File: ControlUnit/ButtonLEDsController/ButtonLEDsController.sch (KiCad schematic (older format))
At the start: 37 parts, among them J1 Conn_01x02_Female, Q1 IRLZ34N, T1 -PNP-2C-BCE, T10 MPSA42-NPN-TO92-CBE, T2 MPSA42-NPN-TO92-CBE, T3 MPSA42-NPN-TO92-CBE, T4 MPSA42-NPN-TO92-CBE, T5 MPSA42-NPN-TO92-CBE, T6 MPSA42-NPN-TO92-CBE, T7 MPSA42-NPN-TO92-CBE, T8 MPSA42-NPN-TO92-CBE, T9 MPSA42-NPN-TO92-CBE, U1 NodeMCU1.0(ESP-12E)

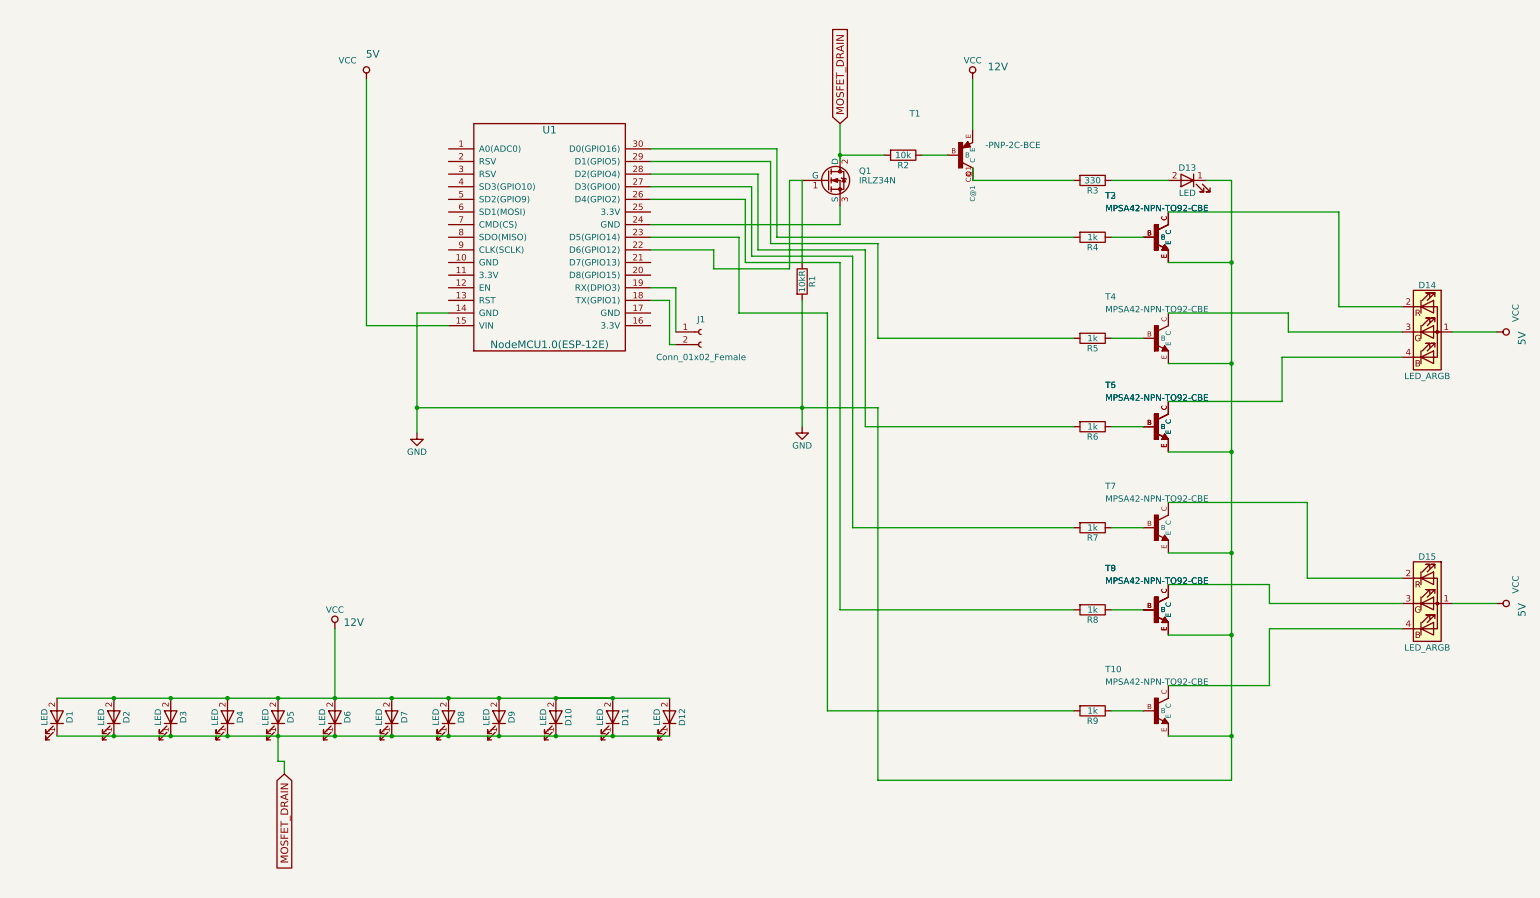
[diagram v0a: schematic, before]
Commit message: transistors in schematic taken from 3rd party lib were bad idea because default kicad footprints wouldn't match the pin references in the schematic (were E,B,C - needed to be 1,2,3 instead)
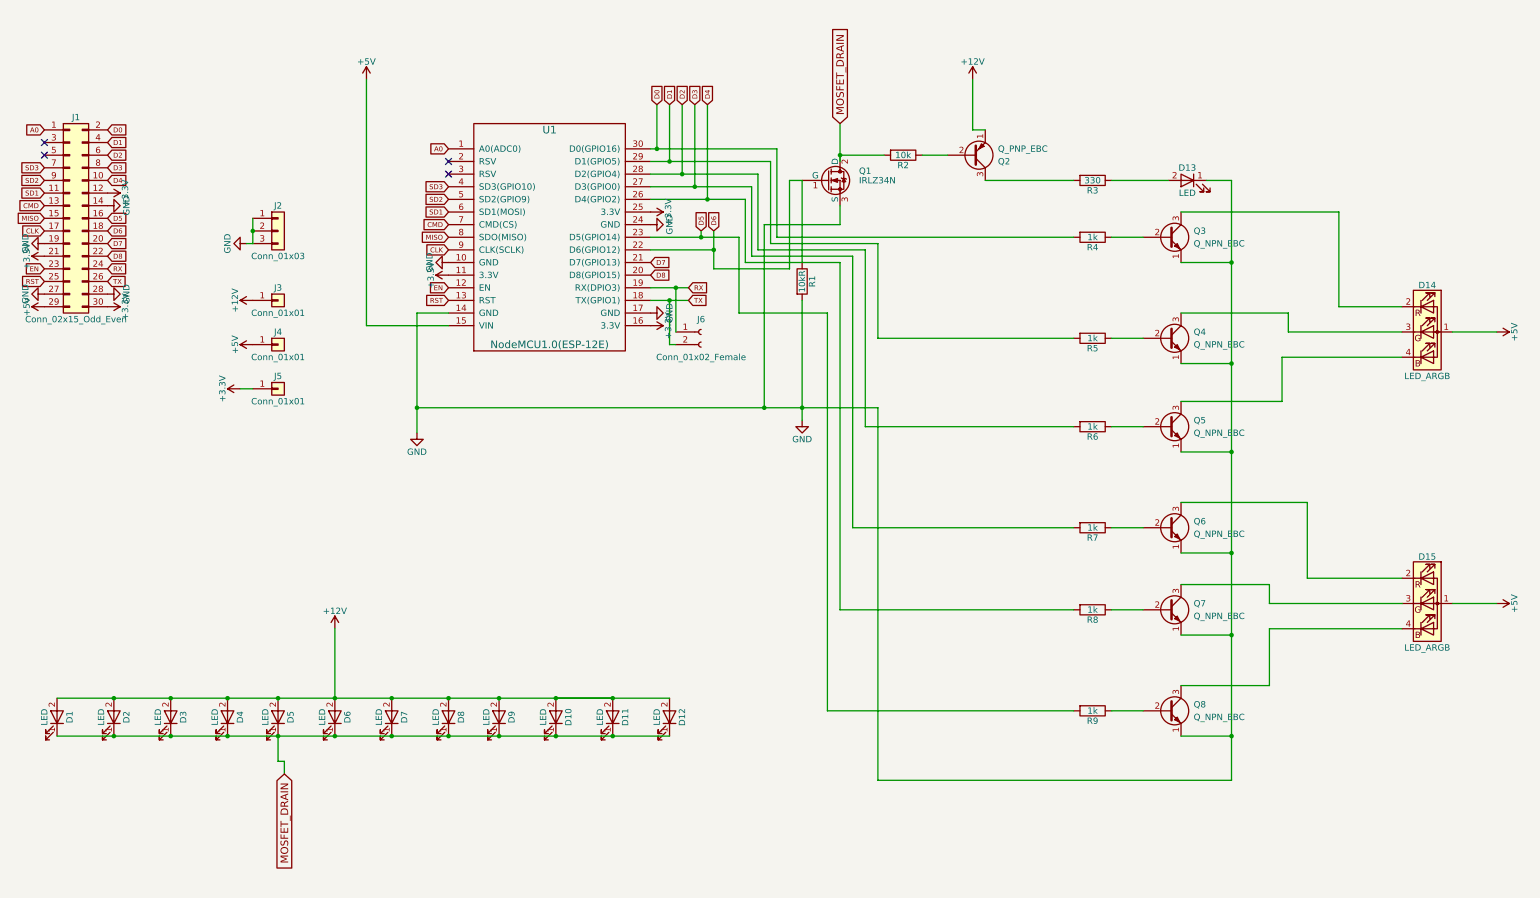
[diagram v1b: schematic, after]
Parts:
- removed T1: -PNP-2C-BCE, transistor-SOT89-BCE, symbol -PNP-2C-BCE
- removed T10, T2, T3, T4, T5, T6, T7, T8, T9: MPSA42-NPN-TO92-CBE, transistor-TO92-CBE, symbol MPSA42-NPN-TO92-CBE
- added J1: Conn_02x15_Odd_Even, Pin_Headers:Pin_Header_Straight_2x15_Pitch2.54mm, symbol Conn_02x15_Odd_Even
- added J2: Conn_01x03, Pin_Headers:Pin_Header_Straight_1x03_Pitch2.54mm, symbol Conn_01x03
- added J3, J4, J5: Conn_01x01, Pin_Headers:Pin_Header_Straight_1x01_Pitch2.54mm, symbol Conn_01x01
- added Q2: Q_PNP_EBC, TO_SOT_Packages_THT:TO-92_Molded_Narrow, symbol Q_PNP_EBC
- added Q3, Q4, Q5, Q6, Q7, Q8: Q_NPN_EBC, TO_SOT_Packages_THT:TO-92_Molded_Narrow, symbol Q_NPN_EBC
- J6: renamed from J1; footprint Socket_Strips:Socket_Strip_Straight_1x02_Pitch2.00mm -> Socket_Strips:Socket_Strip_Straight_1x02_Pitch2.54mm
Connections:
- net GND: now also Q1.3 (S), U1.10 (GND), U1.17 (GND), U1.24 (GND), J1.14 (Pin_14), J1.19 (Pin_19), J1.27 (Pin_27), J1.28 (Pin_28), J2.1 (Pin_1), J2.2 (Pin_2), J2.3 (Pin_3), Q3.1 (E), Q4.1 (E), Q5.1 (E), Q6.1 (E), Q7.1 (E), Q8.1 (E)
- net A0: now reaches U1.1 (A0(ADC0))
- net A0: now also J1.1 (Pin_1)
- net +3V3: now reaches U1.11 (3.3V)
- net +3V3: now also U1.16 (3.3V), U1.25 (3.3V), J1.12 (Pin_12), J1.21 (Pin_21), J1.30 (Pin_30), J5.1 (Pin_1)
- net EN: now reaches U1.12 (EN)
- net EN: now also J1.23 (Pin_23)
- net RST: now reaches U1.13 (RST)
- net RST: now also J1.25 (Pin_25)
- net TX: now reaches J6.2 (Pin_2), U1.18 (TX(GPIO1))
- net TX: now also J1.26 (Pin_26)
- net RX: now reaches J6.1 (Pin_1), U1.19 (RX(DPIO3))
- net RX: now also J1.24 (Pin_24)
- net D8: now reaches U1.20 (D8(GPIO15))
- net D8: now also J1.22 (Pin_22)
- net D7: now reaches U1.21 (D7(GPIO13))
- net D7: now also J1.20 (Pin_20)
- net D6: now reaches Q1.1 (G), R1.1, U1.22 (D6(GPIO12))
- net D6: now also J1.18 (Pin_18)
- net D5: now reaches R9.2, U1.23 (D5(GPIO14))
- net D5: now also J1.16 (Pin_16)
- net D4: now reaches R8.2, U1.26 (D4(GPIO2))
- net D4: now also J1.10 (Pin_10)
- net D3: now reaches R7.2, U1.27 (D3(GPIO0))
- net D3: now also J1.8 (Pin_8)
- net D2: now reaches R6.2, U1.28 (D2(GPIO4))
- net D2: now also J1.6 (Pin_6)
- net D1: now reaches R5.2, U1.29 (D1(GPIO5))
- net D1: now also J1.4 (Pin_4)
- net D0: now reaches R4.2, U1.30 (D0(GPIO16))
- net D0: now also J1.2 (Pin_2)
- net SD3: now reaches U1.4 (SD3(GPIO10))
- net SD3: now also J1.7 (Pin_7)
- net SD2: now reaches U1.5 (SD2(GPIO9))
- net SD2: now also J1.9 (Pin_9)
- net SD1: now reaches U1.6 (SD1(MOSI))
- net SD1: now also J1.11 (Pin_11)
- net CMD: now reaches U1.7 (CMD(CS))
- net CMD: now also J1.13 (Pin_13)
- net MISO: now reaches U1.8 (SDO(MISO))
- net MISO: now also J1.15 (Pin_15)
- net CLK: now reaches U1.9 (CLK(SCLK))
- net CLK: now also J1.17 (Pin_17)
- net at R2.1: now also Q2.2 (B)
- net at R3.2: now also Q2.3 (C)
- net at R4.1: now also Q3.2 (B)
- net at D14.2 (RK): now also Q3.3 (C)
- net at R5.1: now also Q4.2 (B)
- net at D14.3 (GK): now also Q4.3 (C)
- net at R6.1: now also Q5.2 (B)
- net at D14.4 (BK): now also Q5.3 (C)
- net at R7.1: now also Q6.2 (B)
- net at D15.2 (RK): now also Q6.3 (C)
- net at R8.1: now also Q7.2 (B)
- net at D15.3 (GK): now also Q7.3 (C)
- net at R9.1: now also Q8.2 (B)
- net at D15.4 (BK): now also Q8.3 (C)
- net VCC renamed +12V
- net +12V: now also J3.1 (Pin_1), Q2.1 (E); no longer D14.1 (A), D15.1 (A), U1.15 (VIN)
- new net +5V: D14.1 (A), D15.1 (A), J1.29 (Pin_29), J4.1 (Pin_1), U1.15 (VIN)
- no-connect marks 0 -> 4
